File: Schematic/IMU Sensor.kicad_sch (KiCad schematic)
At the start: 17 parts, among them J18 IMU_nRESET, J19 IMU_INT, U21 BNO086, Y1 32.768 kHz

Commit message: 1st Schematic Review
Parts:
- Y1: value 32.768 kHz -> 32.768k
- renumbered C191 to C201, C192 to C202, C195 to C203, C196 to C204, C197 to C205, C193 to C206, C194 to C207, D49 to D54, J18 to J28, J19 to J29, R157 to R160, R155 to R161, R153 to R162, R151 to R163, R152 to R164, U21 to U25
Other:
- note added: "MAX Current draw is 14.34mA"
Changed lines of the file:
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@@
 		)
 	)
+	(text "MAX Current draw is 14.34mA"
+		(exclude_from_sim no)
+		(at 151.13 121.666 0)
+		(effects
+			(font
+				(size 1.27 1.27)
+			)
+		)
+	)
 	(text "PAGE55: reflow soldering with a peak temperature up to 260°C"
 		(exclude_from_sim no)
@@
 		(on_board yes)
 		(dnp no)
-		(property "Reference" "R153"
+		(property "Reference" "R162"
 			(at 100.076 87.884 90)
 			(effects
@@
 			(project "STAR"
 				(path "/fc8533bc-25dd-4c20-9b4c-ffebebd6739b/93231d0a-659f-4d39-8e8d-78b96a3896a1/75e06a36-2807-4a4b-af1f-d37310ed1ba6"
-					(reference "R153")
+					(reference "R162")
 					(unit 1)
 				)
@@
 		(on_board yes)
 		(dnp no)
-		(property "Reference" "R152"
+		(property "Reference" "R164"
 			(at 188.976 113.284 90)
 			(effects
@@
 			(project "STAR"
 				(path "/fc8533bc-25dd-4c20-9b4c-ffebebd6739b/93231d0a-659f-4d39-8e8d-78b96a3896a1/75e06a36-2807-4a4b-af1f-d37310ed1ba6"
-					(reference "R152")
+					(reference "R164")
 					(unit 1)
 				)
@@
 		(on_board yes)
 		(dnp no)
-		(property "Reference" "#PWR0100"
+		(property "Reference" "#PWR0110"
 			(at 194.31 88.9 0)
 			(effects
@@
 			(project "STAR"
 				(path "/fc8533bc-25dd-4c20-9b4c-ffebebd6739b/93231d0a-659f-4d39-8e8d-78b96a3896a1/75e06a36-2807-4a4b-af1f-d37310ed1ba6"
-					(reference "#PWR0100")
+					(reference "#PWR0110")
 					(unit 1)
 				)
@@
 		(on_board yes)
 		(dnp no)
-		(property "Reference" "U21"
+		(property "Reference" "U25"
 			(at 176.022 74.93 0)
 			(effects
@@
 			(project ""
 				(path "/fc8533bc-25dd-4c20-9b4c-ffebebd6739b/93231d0a-659f-4d39-8e8d-78b96a3896a1/75e06a36-2807-4a4b-af1f-d37310ed1ba6"
-					(reference "U21")
+					(reference "U25")
 					(unit 1)
 				)
@@
 		(on_board yes)
 		(dnp no)
-		(property "Reference" "C193"
+		(property "Reference" "C206"
 			(at 251.714 90.678 0)
 			(effects
@@
 			(project "STAR"
 				(path "/fc8533bc-25dd-4c20-9b4c-ffebebd6739b/93231d0a-659f-4d39-8e8d-78b96a3896a1/75e06a36-2807-4a4b-af1f-d37310ed1ba6"
-					(reference "C193")
+					(reference "C206")
 					(unit 1)
 				)
@@
 		(on_board yes)
 		(dnp no)
-		(property "Reference" "C195"
+		(property "Reference" "C203"
 			(at 103.886 100.33 90)
 			(effects
@@
 			(project "STAR"
 				(path "/fc8533bc-25dd-4c20-9b4c-ffebebd6739b/93231d0a-659f-4d39-8e8d-78b96a3896a1/75e06a36-2807-4a4b-af1f-d37310ed1ba6"
-					(reference "C195")
+					(reference "C203")
 					(unit 1)
 				)
@@
 		(on_board yes)
 		(dnp no)
-		(property "Reference" "R157"
+		(property "Reference" "R160"
 			(at 48.514 88.138 0)
 			(effects
@@
 			(project "STAR"
 				(path "/fc8533bc-25dd-4c20-9b4c-ffebebd6739b/93231d0a-659f-4d39-8e8d-78b96a3896a1/75e06a36-2807-4a4b-af1f-d37310ed1ba6"
-					(reference "R157")
+					(reference "R160")
 					(unit 1)
 				)
@@
 		(on_board yes)
 		(dnp no)
-		(property "Reference" "D49"
+		(property "Reference" "D54"
 			(at 49.784 99.314 90)
 			(effects
@@
 			(project "STAR"
 				(path "/fc8533bc-25dd-4c20-9b4c-ffebebd6739b/93231d0a-659f-4d39-8e8d-78b96a3896a1/75e06a36-2807-4a4b-af1f-d37310ed1ba6"
-					(reference "D49")
+					(reference "D54")
 					(unit 1)
 				)
@@
 		(on_board yes)
 		(dnp no)
-		(property "Reference" "#PWR097"
+		(property "Reference" "#PWR0109"
 			(at 106.68 83.82 0)
 			(effects
@@
 			(project "STAR"
 				(path "/fc8533bc-25dd-4c20-9b4c-ffebebd6739b/93231d0a-659f-4d39-8e8d-78b96a3896a1/75e06a36-2807-4a4b-af1f-d37310ed1ba6"
-					(reference "#PWR097")
+					(reference "#PWR0109")
 					(unit 1)
 				)
@@
 		(on_board yes)
 		(dnp no)
-		(property "Reference" "J18"
+		(property "Reference" "J28"
 			(at 112.014 138.684 0)
 			(effects
@@
 			(project "STAR"
 				(path "/fc8533bc-25dd-4c20-9b4c-ffebebd6739b/93231d0a-659f-4d39-8e8d-78b96a3896a1/75e06a36-2807-4a4b-af1f-d37310ed1ba6"
-					(reference "J18")
+					(reference "J28")
 					(unit 1)
 				)
@@
 		(on_board yes)
 		(dnp no)
-		(property "Reference" "C192"
+		(property "Reference" "C202"
 			(at 80.264 89.408 0)
 			(effects
@@
 			(project "STAR"
 				(path "/fc8533bc-25dd-4c20-9b4c-ffebebd6739b/93231d0a-659f-4d39-8e8d-78b96a3896a1/75e06a36-2807-4a4b-af1f-d37310ed1ba6"
-					(reference "C192")
+					(reference "C202")
 					(unit 1)
 				)
@@
 		(on_board yes)
 		(dnp no)
-		(property "Reference" "J19"
+		(property "Reference" "J29"
 			(at 112.014 152.654 0)
 			(effects
@@
 			(project "STAR"
 				(path "/fc8533bc-25dd-4c20-9b4c-ffebebd6739b/93231d0a-659f-4d39-8e8d-78b96a3896a1/75e06a36-2807-4a4b-af1f-d37310ed1ba6"
-					(reference "J19")
+					(reference "J29")
 					(unit 1)
 				)
@@
 		(on_board yes)
 		(dnp no)
-		(property "Reference" "R151"
+		(property "Reference" "R163"
 			(at 188.976 110.744 90)
 			(effects
@@
 			(project "STAR"
 				(path "/fc8533bc-25dd-4c20-9b4c-ffebebd6739b/93231d0a-659f-4d39-8e8d-78b96a3896a1/75e06a36-2807-4a4b-af1f-d37310ed1ba6"
-					(reference "R151")
+					(reference "R163")
 					(unit 1)
 				)
@@
 		(on_board yes)
 		(dnp no)
-		(property "Reference" "C196"
+		(property "Reference" "C204"
 			(at 218.694 90.678 0)
 			(effects
@@
 			(project "STAR"
 				(path "/fc8533bc-25dd-4c20-9b4c-ffebebd6739b/93231d0a-659f-4d39-8e8d-78b96a3896a1/75e06a36-2807-4a4b-af1f-d37310ed1ba6"
-					(reference "C196")
+					(reference "C204")
 					(unit 1)
 				)
@@
 		(on_board yes)
 		(dnp no)
-		(property "Reference" "#PWR098"
+		(property "Reference" "#PWR0108"
 			(at 72.39 121.92 0)
 			(effects
@@
 			(project "STAR"
 				(path "/fc8533bc-25dd-4c20-9b4c-ffebebd6739b/93231d0a-659f-4d39-8e8d-78b96a3896a1/75e06a36-2807-4a4b-af1f-d37310ed1ba6"
-					(reference "#PWR098")
+					(reference "#PWR0108")
 					(unit 1)
 				)
@@
 		(on_board yes)
 		(dnp no)
-		(property "Reference" "C197"
+		(property "Reference" "C205"
 			(at 239.014 90.678 0)
 			(effects
@@
 			(project "STAR"
 				(path "/fc8533bc-25dd-4c20-9b4c-ffebebd6739b/93231d0a-659f-4d39-8e8d-78b96a3896a1/75e06a36-2807-4a4b-af1f-d37310ed1ba6"
-					(reference "C197")
+					(reference "C205")
 					(unit 1)
 				)
@@
 		(on_board yes)
 		(dnp no)
-		(property "Reference" "R155"
+		(property "Reference" "R161"
 			(at 93.726 145.034 90)
 			(effects
@@
 			(project "STAR"
 				(path "/fc8533bc-25dd-4c20-9b4c-ffebebd6739b/93231d0a-659f-4d39-8e8d-78b96a3896a1/75e06a36-2807-4a4b-af1f-d37310ed1ba6"
-					(reference "R155")
+					(reference "R161")
 					(unit 1)
 				)
@@
 		(on_board yes)
 		(dnp no)
-		(property "Reference" "C194"
+		(property "Reference" "C207"
 			(at 259.334 90.678 0)
 			(effects
@@
 			(project "STAR"
 				(path "/fc8533bc-25dd-4c20-9b4c-ffebebd6739b/93231d0a-659f-4d39-8e8d-78b96a3896a1/75e06a36-2807-4a4b-af1f-d37310ed1ba6"
-					(reference "C194")
+					(reference "C207")
 					(unit 1)
 				)
@@
 		(on_board yes)
 		(dnp no)
-		(property "Reference" "#PWR099"
+		(property "Reference" "#PWR0111"
 			(at 259.08 124.46 0)
 			(effects
@@
 			(project "STAR"
 				(path "/fc8533bc-25dd-4c20-9b4c-ffebebd6739b/93231d0a-659f-4d39-8e8d-78b96a3896a1/75e06a36-2807-4a4b-af1f-d37310ed1ba6"
-					(reference "#PWR099")
+					(reference "#PWR0111")
 					(unit 1)
 				)
@@
 		(on_board yes)
 		(dnp no)
-		(property "Reference" "C191"
+		(property "Reference" "C201"
 			(at 72.644 89.408 0)
 			(effects
@@
 			(project "STAR"
 				(path "/fc8533bc-25dd-4c20-9b4c-ffebebd6739b/93231d0a-659f-4d39-8e8d-78b96a3896a1/75e06a36-2807-4a4b-af1f-d37310ed1ba6"
-					(reference "C191")
+					(reference "C201")
 					(unit 1)
 				)
@@
 			)
 		)
-		(property "Value" "32.768 kHz"
+		(property "Value" "32.768k"
 			(at 230.124 82.804 0)
 			(effects

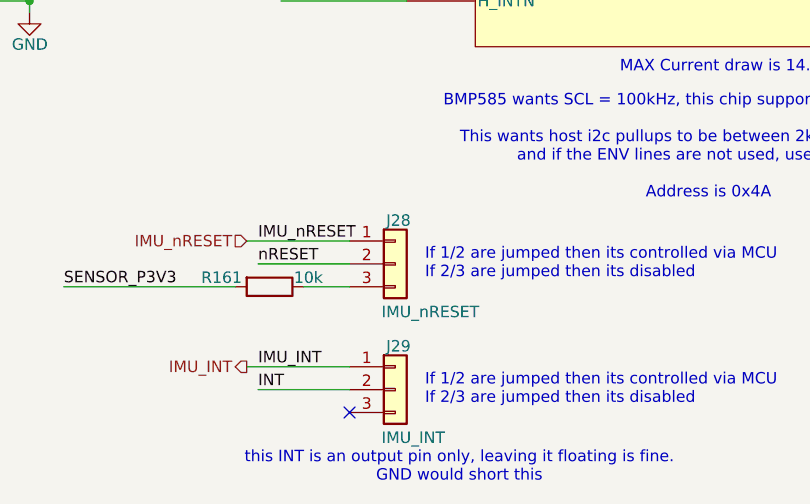
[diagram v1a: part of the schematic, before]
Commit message: added so many test points
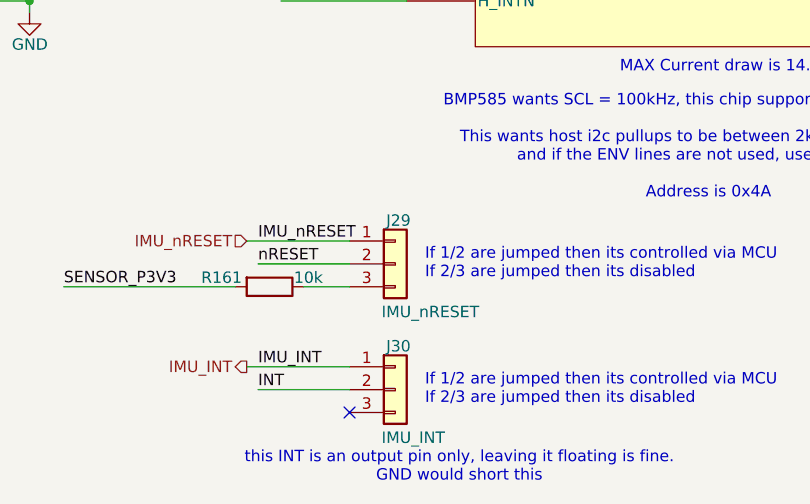
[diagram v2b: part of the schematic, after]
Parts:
- renumbered J28 to J29, J29 to J30
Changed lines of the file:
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@@
 		(on_board yes)
 		(dnp no)
-		(property "Reference" "#PWR0110"
+		(property "Reference" "#PWR0111"
 			(at 194.31 88.9 0)
 			(effects
@@
 			(project "STAR"
 				(path "/fc8533bc-25dd-4c20-9b4c-ffebebd6739b/93231d0a-659f-4d39-8e8d-78b96a3896a1/75e06a36-2807-4a4b-af1f-d37310ed1ba6"
-					(reference "#PWR0110")
+					(reference "#PWR0111")
 					(unit 1)
 				)
@@
 		(on_board yes)
 		(dnp no)
-		(property "Reference" "#PWR0109"
+		(property "Reference" "#PWR0110"
 			(at 106.68 83.82 0)
 			(effects
@@
 			(project "STAR"
 				(path "/fc8533bc-25dd-4c20-9b4c-ffebebd6739b/93231d0a-659f-4d39-8e8d-78b96a3896a1/75e06a36-2807-4a4b-af1f-d37310ed1ba6"
-					(reference "#PWR0109")
+					(reference "#PWR0110")
 					(unit 1)
 				)
@@
 		(on_board yes)
 		(dnp no)
-		(property "Reference" "J28"
+		(property "Reference" "J29"
 			(at 112.014 138.684 0)
 			(effects
@@
 			(project "STAR"
 				(path "/fc8533bc-25dd-4c20-9b4c-ffebebd6739b/93231d0a-659f-4d39-8e8d-78b96a3896a1/75e06a36-2807-4a4b-af1f-d37310ed1ba6"
-					(reference "J28")
+					(reference "J29")
 					(unit 1)
 				)
@@
 		(on_board yes)
 		(dnp no)
-		(property "Reference" "J29"
+		(property "Reference" "J30"
 			(at 112.014 152.654 0)
 			(effects
@@
 			(project "STAR"
 				(path "/fc8533bc-25dd-4c20-9b4c-ffebebd6739b/93231d0a-659f-4d39-8e8d-78b96a3896a1/75e06a36-2807-4a4b-af1f-d37310ed1ba6"
-					(reference "J29")
+					(reference "J30")
 					(unit 1)
 				)
@@
 		(on_board yes)
 		(dnp no)
-		(property "Reference" "#PWR0108"
+		(property "Reference" "#PWR0109"
 			(at 72.39 121.92 0)
 			(effects
@@
 			(project "STAR"
 				(path "/fc8533bc-25dd-4c20-9b4c-ffebebd6739b/93231d0a-659f-4d39-8e8d-78b96a3896a1/75e06a36-2807-4a4b-af1f-d37310ed1ba6"
-					(reference "#PWR0108")
+					(reference "#PWR0109")
 					(unit 1)
 				)
@@
 		(on_board yes)
 		(dnp no)
-		(property "Reference" "#PWR0111"
+		(property "Reference" "#PWR0112"
 			(at 259.08 124.46 0)
 			(effects
@@
 			(project "STAR"
 				(path "/fc8533bc-25dd-4c20-9b4c-ffebebd6739b/93231d0a-659f-4d39-8e8d-78b96a3896a1/75e06a36-2807-4a4b-af1f-d37310ed1ba6"
-					(reference "#PWR0111")
+					(reference "#PWR0112")
 					(unit 1)
 				)

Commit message: updates
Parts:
- renumbered C201 to C203, C202 to C204, C203 to C205, C204 to C206, C205 to C207, C206 to C208, C207 to C209, D54 to D56, J29 to J31, J30 to J32, R160 to R173, R161 to R174, R162 to R175, R163 to R176, R164 to R177
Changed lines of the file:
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@@
 		(on_board yes)
 		(dnp no)
-		(property "Reference" "R162"
+		(property "Reference" "R175"
 			(at 100.076 87.884 90)
 			(effects
@@
 			(project "STAR"
 				(path "/fc8533bc-25dd-4c20-9b4c-ffebebd6739b/93231d0a-659f-4d39-8e8d-78b96a3896a1/75e06a36-2807-4a4b-af1f-d37310ed1ba6"
-					(reference "R162")
+					(reference "R175")
 					(unit 1)
 				)
@@
 		(on_board yes)
 		(dnp no)
-		(property "Reference" "R164"
+		(property "Reference" "R177"
 			(at 188.976 113.284 90)
 			(effects
@@
 			(project "STAR"
 				(path "/fc8533bc-25dd-4c20-9b4c-ffebebd6739b/93231d0a-659f-4d39-8e8d-78b96a3896a1/75e06a36-2807-4a4b-af1f-d37310ed1ba6"
-					(reference "R164")
+					(reference "R177")
 					(unit 1)
 				)
@@
 		(on_board yes)
 		(dnp no)
-		(property "Reference" "#PWR0111"
+		(property "Reference" "#PWR0113"
 			(at 194.31 88.9 0)
 			(effects
@@
 			(project "STAR"
 				(path "/fc8533bc-25dd-4c20-9b4c-ffebebd6739b/93231d0a-659f-4d39-8e8d-78b96a3896a1/75e06a36-2807-4a4b-af1f-d37310ed1ba6"
-					(reference "#PWR0111")
+					(reference "#PWR0113")
 					(unit 1)
 				)
@@
 		(on_board yes)
 		(dnp no)
-		(property "Reference" "C206"
+		(property "Reference" "C208"
 			(at 251.714 90.678 0)
 			(effects
@@
 			(project "STAR"
 				(path "/fc8533bc-25dd-4c20-9b4c-ffebebd6739b/93231d0a-659f-4d39-8e8d-78b96a3896a1/75e06a36-2807-4a4b-af1f-d37310ed1ba6"
-					(reference "C206")
+					(reference "C208")
 					(unit 1)
 				)
@@
 		(on_board yes)
 		(dnp no)
-		(property "Reference" "C203"
+		(property "Reference" "C205"
 			(at 103.886 100.33 90)
 			(effects
@@
 			(project "STAR"
 				(path "/fc8533bc-25dd-4c20-9b4c-ffebebd6739b/93231d0a-659f-4d39-8e8d-78b96a3896a1/75e06a36-2807-4a4b-af1f-d37310ed1ba6"
-					(reference "C203")
+					(reference "C205")
 					(unit 1)
 				)
@@
 		(on_board yes)
 		(dnp no)
-		(property "Reference" "R160"
+		(property "Reference" "R173"
 			(at 48.514 88.138 0)
 			(effects
@@
 			(project "STAR"
 				(path "/fc8533bc-25dd-4c20-9b4c-ffebebd6739b/93231d0a-659f-4d39-8e8d-78b96a3896a1/75e06a36-2807-4a4b-af1f-d37310ed1ba6"
-					(reference "R160")
+					(reference "R173")
 					(unit 1)
 				)
@@
 		(on_board yes)
 		(dnp no)
-		(property "Reference" "D54"
+		(property "Reference" "D56"
 			(at 49.784 99.314 90)
 			(effects
@@
 			(project "STAR"
 				(path "/fc8533bc-25dd-4c20-9b4c-ffebebd6739b/93231d0a-659f-4d39-8e8d-78b96a3896a1/75e06a36-2807-4a4b-af1f-d37310ed1ba6"
-					(reference "D54")
+					(reference "D56")
 					(unit 1)
 				)
@@
 		(on_board yes)
 		(dnp no)
-		(property "Reference" "#PWR0110"
+		(property "Reference" "#PWR0112"
 			(at 106.68 83.82 0)
 			(effects
@@
 			(project "STAR"
 				(path "/fc8533bc-25dd-4c20-9b4c-ffebebd6739b/93231d0a-659f-4d39-8e8d-78b96a3896a1/75e06a36-2807-4a4b-af1f-d37310ed1ba6"
-					(reference "#PWR0110")
+					(reference "#PWR0112")
 					(unit 1)
 				)
@@
 		(on_board yes)
 		(dnp no)
-		(property "Reference" "J29"
+		(property "Reference" "J31"
 			(at 112.014 138.684 0)
 			(effects
@@
 			(project "STAR"
 				(path "/fc8533bc-25dd-4c20-9b4c-ffebebd6739b/93231d0a-659f-4d39-8e8d-78b96a3896a1/75e06a36-2807-4a4b-af1f-d37310ed1ba6"
-					(reference "J29")
+					(reference "J31")
 					(unit 1)
 				)
@@
 		(on_board yes)
 		(dnp no)
-		(property "Reference" "C202"
+		(property "Reference" "C204"
 			(at 80.264 89.408 0)
 			(effects
@@
 			(project "STAR"
 				(path "/fc8533bc-25dd-4c20-9b4c-ffebebd6739b/93231d0a-659f-4d39-8e8d-78b96a3896a1/75e06a36-2807-4a4b-af1f-d37310ed1ba6"
-					(reference "C202")
+					(reference "C204")
 					(unit 1)
 				)
@@
 		(on_board yes)
 		(dnp no)
-		(property "Reference" "J30"
+		(property "Reference" "J32"
 			(at 112.014 152.654 0)
 			(effects
@@
 			(project "STAR"
 				(path "/fc8533bc-25dd-4c20-9b4c-ffebebd6739b/93231d0a-659f-4d39-8e8d-78b96a3896a1/75e06a36-2807-4a4b-af1f-d37310ed1ba6"
-					(reference "J30")
+					(reference "J32")
 					(unit 1)
 				)
@@
 		(on_board yes)
 		(dnp no)
-		(property "Reference" "R163"
+		(property "Reference" "R176"
 			(at 188.976 110.744 90)
 			(effects
@@
 			(project "STAR"
 				(path "/fc8533bc-25dd-4c20-9b4c-ffebebd6739b/93231d0a-659f-4d39-8e8d-78b96a3896a1/75e06a36-2807-4a4b-af1f-d37310ed1ba6"
-					(reference "R163")
+					(reference "R176")
 					(unit 1)
 				)
@@
 		(on_board yes)
 		(dnp no)
-		(property "Reference" "C204"
+		(property "Reference" "C206"
 			(at 218.694 90.678 0)
 			(effects
@@
 			(project "STAR"
 				(path "/fc8533bc-25dd-4c20-9b4c-ffebebd6739b/93231d0a-659f-4d39-8e8d-78b96a3896a1/75e06a36-2807-4a4b-af1f-d37310ed1ba6"
-					(reference "C204")
+					(reference "C206")
 					(unit 1)
 				)
@@
 		(on_board yes)
 		(dnp no)
-		(property "Reference" "#PWR0109"
+		(property "Reference" "#PWR0111"
 			(at 72.39 121.92 0)
 			(effects
@@
 			(project "STAR"
 				(path "/fc8533bc-25dd-4c20-9b4c-ffebebd6739b/93231d0a-659f-4d39-8e8d-78b96a3896a1/75e06a36-2807-4a4b-af1f-d37310ed1ba6"
-					(reference "#PWR0109")
+					(reference "#PWR0111")
 					(unit 1)
 				)
@@
 		(on_board yes)
 		(dnp no)
-		(property "Reference" "C205"
+		(property "Reference" "C207"
 			(at 239.014 90.678 0)
 			(effects
@@
 			(project "STAR"
 				(path "/fc8533bc-25dd-4c20-9b4c-ffebebd6739b/93231d0a-659f-4d39-8e8d-78b96a3896a1/75e06a36-2807-4a4b-af1f-d37310ed1ba6"
-					(reference "C205")
+					(reference "C207")
 					(unit 1)
 				)
@@
 		(on_board yes)
 		(dnp no)
-		(property "Reference" "R161"
+		(property "Reference" "R174"
 			(at 93.726 145.034 90)
 			(effects
@@
 			(project "STAR"
 				(path "/fc8533bc-25dd-4c20-9b4c-ffebebd6739b/93231d0a-659f-4d39-8e8d-78b96a3896a1/75e06a36-2807-4a4b-af1f-d37310ed1ba6"
-					(reference "R161")
+					(reference "R174")
 					(unit 1)
 				)
@@
 		(on_board yes)
 		(dnp no)
-		(property "Reference" "C207"
+		(property "Reference" "C209"
 			(at 259.334 90.678 0)
 			(effects
@@
 			(project "STAR"
 				(path "/fc8533bc-25dd-4c20-9b4c-ffebebd6739b/93231d0a-659f-4d39-8e8d-78b96a3896a1/75e06a36-2807-4a4b-af1f-d37310ed1ba6"
-					(reference "C207")
+					(reference "C209")
 					(unit 1)
 				)
@@
 		(on_board yes)
 		(dnp no)
-		(property "Reference" "#PWR0112"
+		(property "Reference" "#PWR0114"
 			(at 259.08 124.46 0)
 			(effects
@@
 			(project "STAR"
 				(path "/fc8533bc-25dd-4c20-9b4c-ffebebd6739b/93231d0a-659f-4d39-8e8d-78b96a3896a1/75e06a36-2807-4a4b-af1f-d37310ed1ba6"
-					(reference "#PWR0112")
+					(reference "#PWR0114")
 					(unit 1)
 				)
@@
 		(on_board yes)
 		(dnp no)
-		(property "Reference" "C201"
+		(property "Reference" "C203"
 			(at 72.644 89.408 0)
 			(effects
@@
 			(project "STAR"
 				(path "/fc8533bc-25dd-4c20-9b4c-ffebebd6739b/93231d0a-659f-4d39-8e8d-78b96a3896a1/75e06a36-2807-4a4b-af1f-d37310ed1ba6"
-					(reference "C201")
+					(reference "C203")
 					(unit 1)
 				)
